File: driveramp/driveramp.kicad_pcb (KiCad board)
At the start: 4 copper layers, 71.1 x 52.1 mm, 21 parts, among them CON1 BARREL_JACK, J1 SMA, J2 SMA, K1 CONN_3, P2 CONN_2, Q1 MRFE6VS25L

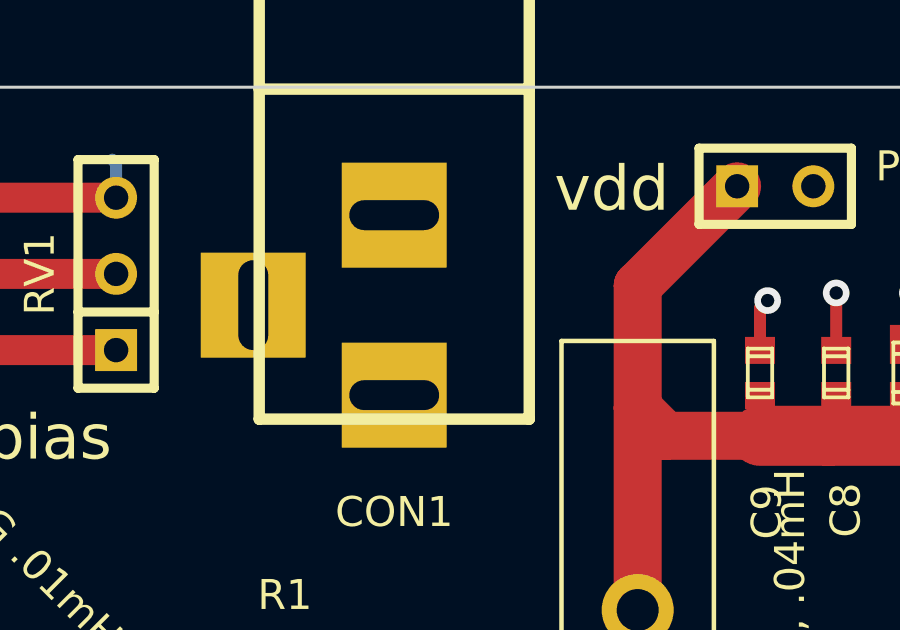
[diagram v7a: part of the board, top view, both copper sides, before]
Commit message: removed high voltage supply from agc board, added missing kicad files
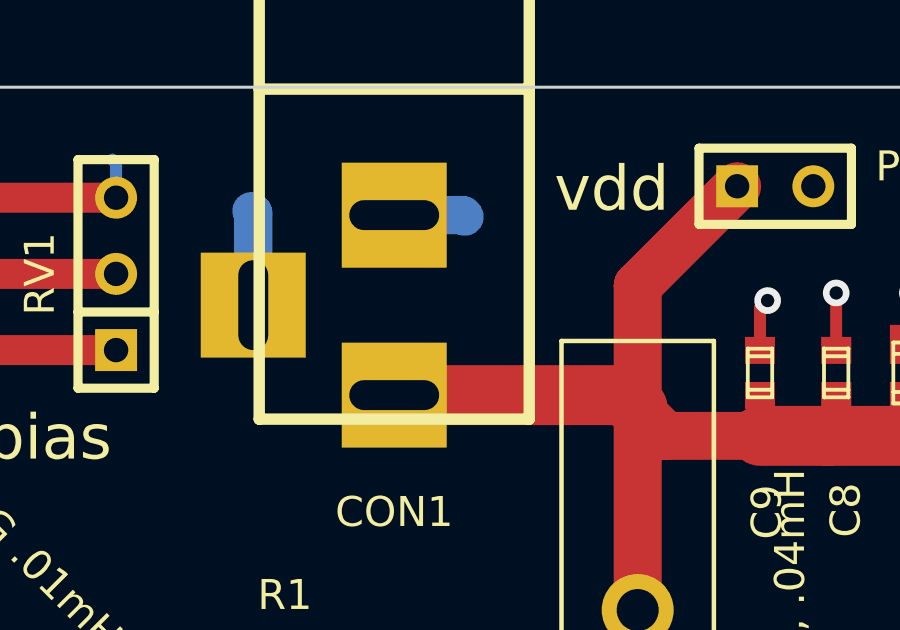
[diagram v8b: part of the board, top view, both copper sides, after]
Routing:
- net /vsupply: track 37.5 -> 45.8 mm
- net GND: track 66.3 -> 71.9 mm
